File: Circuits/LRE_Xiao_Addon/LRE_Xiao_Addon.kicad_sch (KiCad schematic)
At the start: 13 parts, among them J1 Conn_01x06_Socket, J3 Conn_01x06_Socket, J4 Conn_01x02_Pin, Q1 S8050, Q2 S8050, Q3 S8050

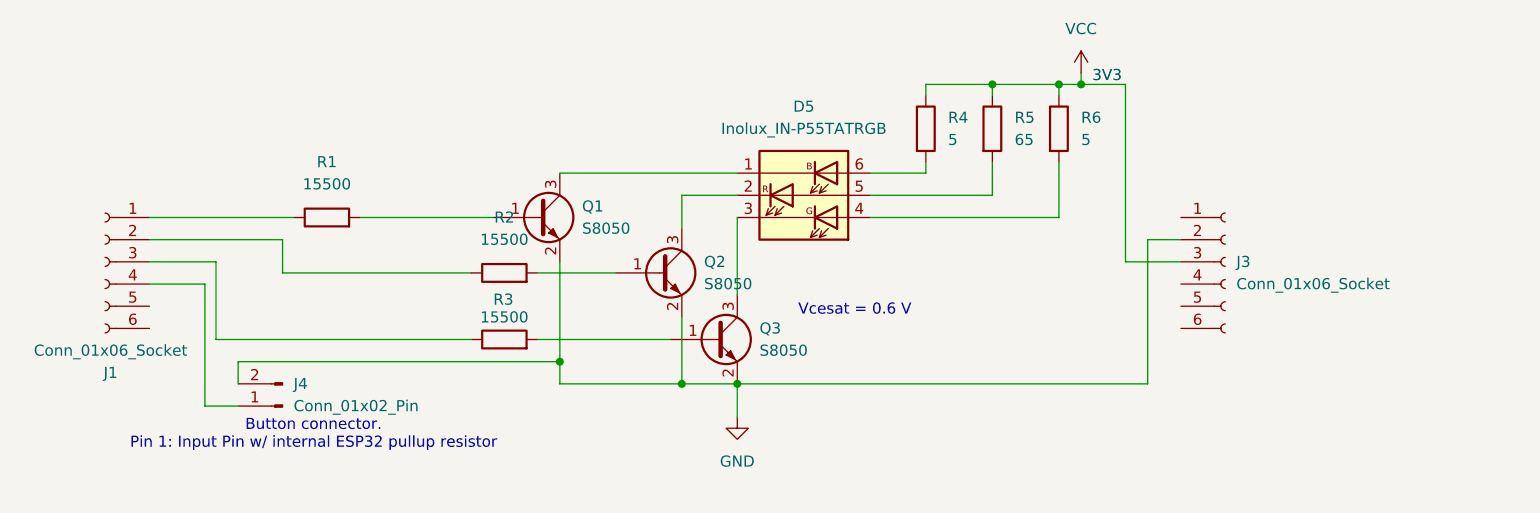
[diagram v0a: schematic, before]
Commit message: PCB changes: RGB Pins moved, voltage div to A0 for measuring batt voltage, voltage div to detect VBUS voltage
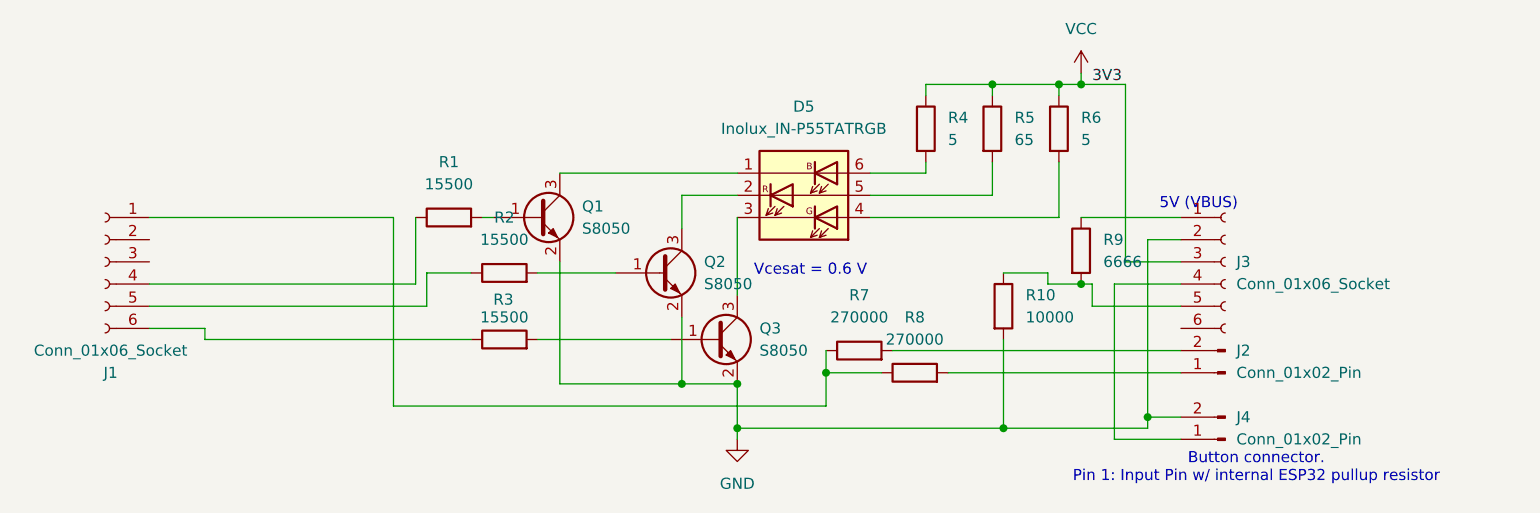
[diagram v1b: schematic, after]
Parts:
- added J2: Conn_01x02_Pin, Connector_PinHeader_2.54mm:PinHeader_1x02_P2.54mm_Vertical, symbol Connector:Conn_01x02_Pin
- added R10: 10000, Resistor_SMD:R_1206_3216Metric_Pad1.30x1.75mm_HandSolder, symbol Device:R
- added R7, R8: 270000, Resistor_SMD:R_1206_3216Metric_Pad1.30x1.75mm_HandSolder, symbol Device:R
- added R9: 6666, Resistor_SMD:R_1206_3216Metric_Pad1.30x1.75mm_HandSolder, symbol Device:R
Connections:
- net GND: now also R10.2
- net at R2.1: now also J1.5 (Pin_5); no longer J1.2 (Pin_2)
- net at R3.1: now also J1.6 (Pin_6); no longer J1.3 (Pin_3)
- net at J4.1 (Pin_1): now also J3.4 (Pin_4); no longer J1.4 (Pin_4)
- net at J3.1 (Pin_1): now also R9.1
- net at J3.5 (Pin_5): now also R10.1, R9.2
- net at J1.1 (Pin_1): now also R7.1, R8.1; no longer R1.1
- new net: J2.2 (Pin_2), R7.2
- new net: J2.1 (Pin_1), R8.2
- new net: J1.4 (Pin_4), R1.1
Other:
- note added: "5V (VBUS)"
- moved on the sheet: J4, R1
